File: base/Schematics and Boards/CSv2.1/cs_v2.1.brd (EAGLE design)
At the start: 38.1 x 44.5 mm, 80 parts, among them J101 J-JTAG-CORTEX-NEEDLE6-LEGS, J301 HIROSE-DF40_44-PIN_CONNECTORS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, J302 HIROSE-DF40_30-PIN_CONNECTORS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, Q201 FK3303010L, Q202 DMG3415UFY4Q-7F, Q203 FK3303010L, Q204 FK3303010L, U101 ATSAMD51, U102 AT25SF641-MHB-T, U201 COULOMB-MAX17262, U202 MAX77827BEWC+T, U203 SENSOR-SI7006, U204 LOADSWITCH-MIC94164, U205 LOADSWITCH-MIC94164, Y101 16M, Y102 ABS07-32.768KHZ-9-T

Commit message: Minor modifications from learnings of debug-board build
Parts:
- DTR, PROC, STOR, TEMP: value TPTP06R -> PTR1TP10SQ; device TestPoints:TP06R -> TestPoints:TP10SQ
- J301: value HIROSE-DF40_44-PIN_CONNECTORS-RECEPTACLE -> HIROSE-DF40_50-PIN_CONNECTORS-RECEPTACLE; device Connectors:HRS_DF40HC(3.0)-44DS-0.4V(51) -> Connectors:HRS_DF40HC(4.0)-50DS-0.4V(51)
- J302: value HIROSE-DF40_30-PIN_CONNECTORS-RECEPTACLE -> HIROSE-DF40_50-PIN_CONNECTORS-RECEPTACLE; device Connectors:HRS_DF40HC(3.0)-30DS-0.4V(51) -> Connectors:HRS_DF40HC(4.0)-50DS-0.4V(51)
- R206: value 1 -> 2.21
- moved J302 3.81 mm to (24.9, 40.5)

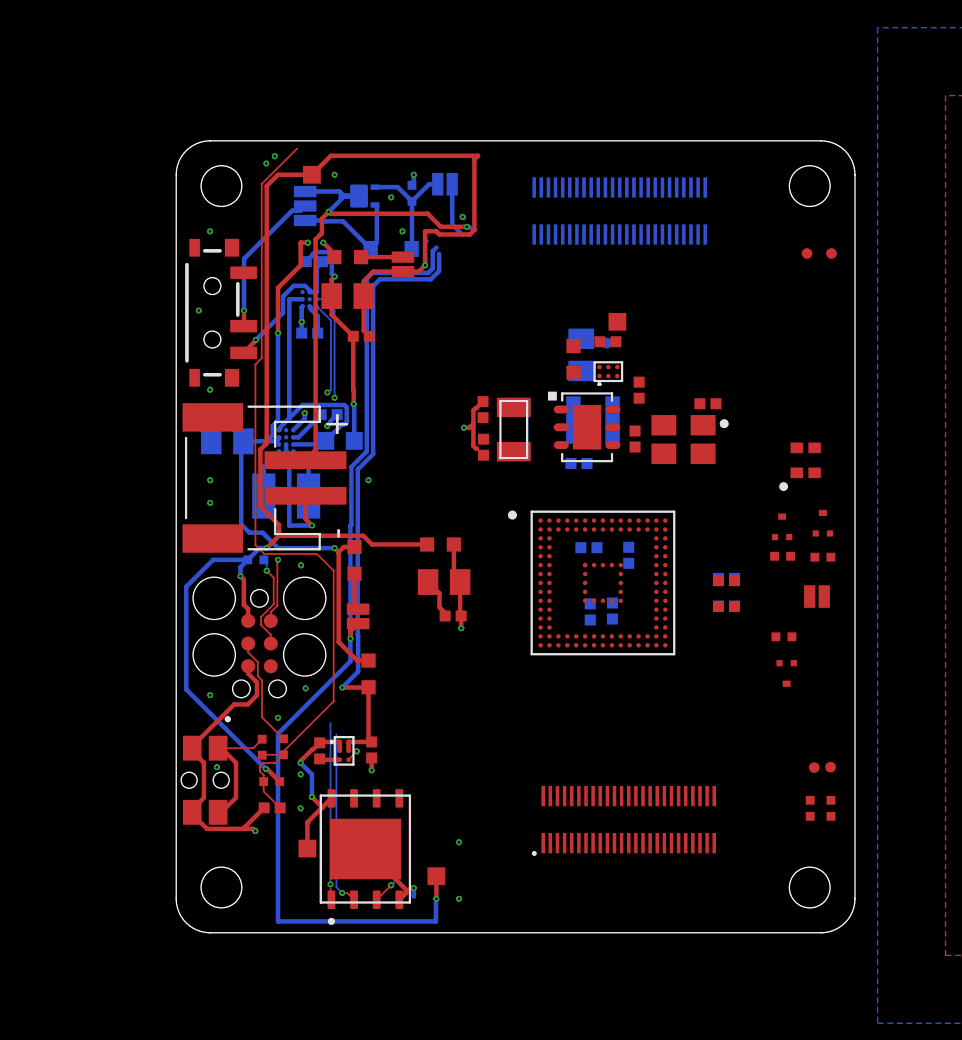
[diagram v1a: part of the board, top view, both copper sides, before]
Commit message: Revision 2.1 of schematic for the CommonSense Main Board
Changes include (at the least): Removal LED NFETs, increase connector size to 50 pins w/ 4mm z-height, swap FLASH for a Winbond part with 1 Gbit NVM, change current measurement to include two daughter card channels, add LDO as alternative to buck-boost with gating solder jumpers, modify power-switching setup to use dual PFET (one is an extension of the mechanical switch to allow higher currents), total revamp of DTR/DBG card pin-mapping, and probably a few more small items. 

These changes are local to the schematic, for the most part. Changes to the board are minimal, but do include shifting the connector up, as well as the top-most drill-holes
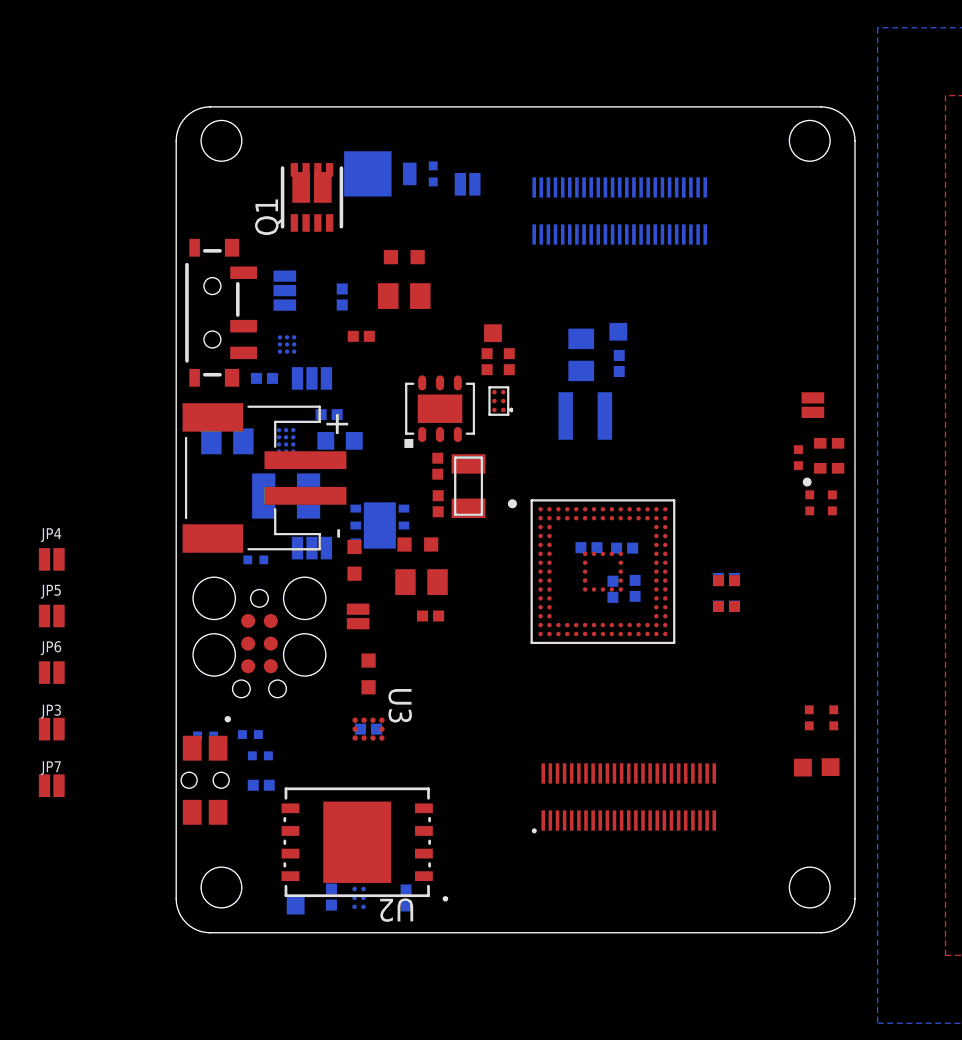
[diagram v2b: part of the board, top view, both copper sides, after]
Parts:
- removed C116, C117: 6.8p, Capacitors:C0402
- removed DTR, PROC: PTR1TP10SQ, TestPoints:TP10SQ
- removed JP204: JUMPER-SMT_2_NC_PASTE_NO-SILK, Connectors:SMT-JUMPER_2_NC_PASTE_NO-SILK
- removed Q201, Q203, Q204: FK3303010L, Switches:SSSMINI3
- removed Q202: DMG3415UFY4Q-7F, Switches:X2-DFN2015-3
- removed R205: 10, Resistors:R0603
- removed RXDBG, TXDBG: TPTP06R, TestPoints:TP06R
- removed U102: AT25SF641-MHB-T, Storage:8-UDFN
- removed Y101: 16M, Oscillators:XTAL_EPSON_TSX3225
- added C1: 0.1u, Capacitors:C0402
- added JP1, JP2: JUMPER-SMT_3_1-NC_PASTE_NO-SILK, SparkFun-Jumpers:SMT-JUMPER_3_1-NC_PASTE_NO-SILK
- added JP3, JP7: JUMPER-SMT_2_NC_PASTE_NO-SILK, Connectors:SMT-JUMPER_2_NC_PASTE_NO-SILK
- added JP4, JP5, JP6: JUMPER-SMT_2_NO_PASTEFREE, Connectors:SMT-JUMPER_2_NO_PASTEFREE_NO-SILK
- added Q1: SIS903DN, Switches:POWERPACK1212_SIS903DN
- added U1: NCP708MU330TAG, Regulators:UDFN6_NCP708]
- added U2: W25N01GVZEIG, Storage:WSON-8_W15N
- added U3: TS3A24159YZPR, Switches:DSBGA10
- CPU, SCL, SDA: value TPTP06R -> PTR1TP10SQ; device TestPoints:TP06R -> TestPoints:TP10SQ
- D201: value CUS520H3F -> MBRM110ET1G; device Diodes:CUS520H3F -> Diodes:DO-216AA_ONS
- moved JP202 10.7 mm to (35.7, 29.6), turned to 90 degrees
- moved C208 9.58 mm to (12.9, 1.96), flipped to the bottom
- moved C206 8.56 mm to (8.71, 2.01), flipped to the bottom
- moved U203 8.32 mm to (14.8, 29.4), turned to 90 degrees
- moved U204 8.30 mm to (10.3, 1.96), flipped to the bottom
- moved R203 7.66 mm to (35.6, 24.1), turned to 270 degrees
- moved C209 7.46 mm to (18.7, 32.1)
- moved TEMP 7.01 mm to (17.8, 33.7)
- moved C207 6.87 mm to (17.4, 32.1), turned to 90 degrees
- moved U205 6.36 mm to (18.1, 29.8), turned to 180 degrees
- moved C103 6.05 mm to (24.9, 32.0), turned to 270 degrees
- moved R204 5.61 mm to (34.9, 26.7), turned to 270 degrees
- moved R103 5.08 mm to (36.9, 12.1), turned to 90 degrees
- moved R104 5.08 mm to (35.5, 12.1), turned to 90 degrees
- moved JP203 4.89 mm to (6.10, 36.0), turned to 270 degrees
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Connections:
- net DTR_V_SENSE- renamed DTR_MSTR_GPIO1
- removed net +3V3_DTR_SENSE: JP205.2, R207.2
- removed net +3V3_PROC_SENSE: JP204.2, R206.2
- removed net +3V3_STOR_SENSE: C206.1, J302.18, R208.2, U204.A2, U204.B2
- removed net +3V3_TEMP_SENSE: C207.1, J302.20, R205.2, U205.A2, U205.B2
- removed net DTR_BUS0_AIN0: J301.8, U101.PA02
- removed net DTR_BUS0_AIN1: J301.16, U101.PA03
- removed net DTR_BUS0_GPIO0: J301.24, U101.PB12
- removed net DTR_BUS0_GPIO1: J301.32, U101.PB13
- removed net DTR_BUS0_SERCOM0_P0: J301.7, U101.PA08
- removed net DTR_BUS0_SERCOM0_P1: J301.15, U101.PA09
- removed net DTR_BUS0_SERCOM0_P2: J301.23, U101.PA10
- removed net DTR_BUS0_SERCOM0_P3: J301.31, U101.PA11
- removed net DTR_BUS1_AIN0: J301.10, U101.PA04
- removed net DTR_BUS1_AIN1: J301.18, U101.PA05
- removed net DTR_BUS2_AIN0: J301.12, U101.PC02
- removed net DTR_BUS2_AIN1: J301.20, U101.PC03
- removed net DTR_BUS3_AIN0: J301.14, U101.PB04
- removed net DTR_BUS3_AIN1: J301.22, U101.PB05
- removed net DTR_BUS3_GPIO0: J301.30, U101.PA06
- removed net DTR_BUS3_GPIO1: J301.38, U101.PA07
- removed net DTR_BUS3_SERCOM7_P0: J301.13, U101.PD08
- removed net DTR_BUS3_SERCOM7_P1: J301.21, U101.PD09
- removed net DTR_BUS3_SERCOM7_P2: J301.29, U101.PD10
- removed net DTR_BUS3_SERCOM7_P3: J301.37, U101.PD11
- removed net DTR_DETECT: J301.39, U101.PA21
- removed net DTR_MASTER_I2C_SCL: J301.40, R103.1, SCL.TP, U101.PA23, U201.B1, U203.6
- removed net DTR_MASTER_I2C_SDA: J301.42, R104.1, SDA.TP, U101.PA22, U201.C1, U203.1
- removed net DTR_MASTER_IRQ: J301.44
- removed net N$16: Q203.3, R203.2
- removed net STOR_HOLD: U101.PB07, U102.7
- removed net STOR_SPI5_MISO: U101.PB03, U102.2
- removed net STOR_SPI5_MOSI: U101.PB00, U102.5
- removed net STOR_SPI5_NCS: U101.PB02, U102.1
- removed net STOR_SPI5_SCK: U101.PB01, U102.6
- removed net STOR_WP: U101.PB06, U102.3
- removed net VDD_DBG: J302.2, J302.4, JP201.2
- removed net VDD_SW_IN: JP203.2, S201.2
- removed net XIN: C116.1, U101.PB22, Y101.1
- removed net XOUT: C117.1, U101.PB23, Y101.3
- new net +3V3_DTR_SENSE-: JP205.2, JP5.2, R207.2, U3.A1, U3.A3, U3.C1
- new net DBG_DTR_V_SENSE: J301.8, J302.18
- new net DBG_DTR_V_SENSE_EX: J302.20, U3.C3
- new net DBG_GPIO10: J302.40, U101.PB28
- new net DBG_GPIO11: J302.38, U101.PB29
- new net DBG_GPIO4/SERCOM6_P0: J302.30, U101.PC16
- new net DBG_GPIO5/SERCOM6_P1: J302.32, U101.PC17
- new net DBG_GPIO6/SERCOM6_P2: J302.34, U101.PC18
- new net DBG_GPIO7/SERCOM6_P3: J302.36, U101.PC19
- new net DBG_GPIO8: J302.44, U101.PB26
- new net DBG_GPIO9: J302.42, U101.PB27
- new net DBG_PROC_V_SENSE: J302.16, JP6.2, JP7.2, R206.2
- new net DBG_STOR_V_SENSE: C206.1, J302.22, JP4.2, R208.2, U204.A2, U204.B2
- new net DBG_VDD: J302.2, J302.4, J302.6, JP201.2
- new net DTR_BUS0_AIN0/GPIO2: J301.7, U101.PA02
- new net DTR_BUS0_AIN1/GPIO3: J301.9, U101.PA03
- new net DTR_BUS0_GPIO0/I2S_SCK0: J301.19, U101.PB16
- new net DTR_BUS0_GPIO1/I2S_MCK0: J301.21, U101.PB17
- new net DTR_BUS0_SERCOM5_P0/I2S_FS1: J301.42, U101.PA23
- new net DTR_BUS0_SERCOM5_P1/I2S_SDI: J301.40, U101.PA22
- new net DTR_BUS0_SERCOM5_P2/I2S_FS0: J301.30, U101.PA20
- new net DTR_BUS0_SERCOM5_P3/I2S_SDO: J301.28, U101.PA21
- new net DTR_BUS1_AIN0/GPIO2: J301.11, U101.PA04
- new net DTR_BUS1_AIN1/GPIO3: J301.13, U101.PA05
- new net DTR_BUS2_AIN0/GPIO2: J301.15, U101.PC02
- new net DTR_BUS2_AIN1/GPIO3: J301.17, U101.PC03
- new net DTR_DETECT/DTR_IRQ0/SERCOM7_P2: J301.16, U101.PD10
- new net DTR_IRQ1/SERCOM7_P3: J301.18, U101.PD11
- new net DTR_MSTR_GPIO0: J301.41, U101.PC15
- new net DTR_MSTR_GPIO_1: U101.PC20
- new net DTR_MSTR_I2C_SCL_SERCOM7_P1: J301.14, R103.1, SCL.TP, U101.PD09, U201.B1, U203.6
- new net DTR_MSTR_I2C_SDA_SERCOM7_P0: J301.12, R104.1, SDA.TP, U101.PD08, U201.C1, U203.1
- new net DTR_MSTR_SPI_CSS0_SERCOM3_P2: J301.37, U101.PD20
- new net DTR_MSTR_SPI_CSS1: J301.31, U101.PD12
- new net DTR_MSTR_SPI_MISO_SERCOM3_P3: J301.39, U101.PD21
- new net DTR_MSTR_SPI_MOSI_SERCOM3_P0: J301.33, U101.PC23
- new net DTR_MSTR_SPI_SCK_SERCOM3_P1: J301.35, U101.PC22
- new net DTR_SENSE_SW: U101.PC07, U3.B1, U3.B3
- new net DTR_V_SENSE_EX: J301.10, U3.D3
- new net N$11: Q1.4, S201.2
- new net N$3: JP2.1, U202.C2, U202.C3
- new net N$7: JP1.3, U1.1, U1.6
- new net N$8: JP203.2, Q1.10, Q1.5, Q1.6, S201.1
- new net STOR_QSPI_CK: U101.PB10, U2.6
- new net STOR_QSPI_CS: U101.PB11, U2.1
- new net STOR_QSPI_D0: U101.PA08, U2.5
- new net STOR_QSPI_D1: U101.PA09, U2.2
- new net STOR_QSPI_D2: U101.PA10, U2.3
- new net STOR_QSPI_D3: U101.PA11, U2.7
- new net VREG_BB_IN: JP1.1, U202.A2, U202.C4
- net +3V3: now also C207.1, J302.14, JP2.2, JP3.2, JP4.1, JP5.1, JP6.1, U205.A2, U205.B2, U3.D1; no longer J302.12, R205.1, U202.C2, U202.C3
- net +3V3_DTR: no longer DTR.TP, J302.16
- net +3V3_PROC: now also JP7.1; no longer J302.14, JP204.1, PROC.TP
- net +3V3_STOR: now also U2.8; no longer U102.8
- net +3V7_BATT: now also J302.12, JP203.1, Q1.7, Q1.8, Q1.9; no longer J302.6, JP203.3, Q202.3-1, Q202.3-2
- net CC_IN: now also Q1.3; no longer S201.1
- net DBG_GPIO0: now also J302.31, U101.PB22; no longer J302.7, U101.PC16
- net DBG_GPIO1: now also J302.29, U101.PB23; no longer J302.9, U101.PC17
- net DBG_GPIO2: now also J302.27, U101.PB24; no longer J302.11, U101.PC18
- net DBG_GPIO3: now also J302.25, U101.PB25; no longer J302.13, U101.PC19
- net DBG_SERIAL_RX_SERCOM4: now also J302.9; no longer J302.17, RXDBG.TP
- net DBG_SERIAL_TX_SERCOM4: now also J302.11; no longer J302.15, TXDBG.TP
- net DBG_SWCLK: now also J302.28; no longer J302.19
- net DBG_SWDIO: now also J302.26; no longer J302.21
- net DBG_TRACE_CLK: now also J302.23; no longer J302.26
- net DBG_TRACE_D0: now also J302.15; no longer J302.23
- net DBG_TRACE_D1: now also J302.17; no longer J302.25
- net DBG_TRACE_D2: now also J302.19; no longer J302.27
- net DBG_TRACE_D3: now also J302.21; no longer J302.29
- net DBG_TRACE_SWO: now also J302.13; no longer J302.28
- net DBG_USB_D_N: now also J302.49; no longer J302.22
- net DBG_USB_D_P: now also J302.47; no longer J302.24
- net DTR_BUS1_GPIO0: now also J301.23, U101.PC11; no longer J301.26, U101.PB14
- net DTR_BUS1_GPIO1: now also J301.25, U101.PC12; no longer J301.34, U101.PB15
- net DTR_BUS1_SERCOM1_P0: now also J301.38; no longer J301.9
- net DTR_BUS1_SERCOM1_P1: now also J301.36; no longer J301.17
- net DTR_BUS1_SERCOM1_P2: now also J301.26; no longer J301.25
- net DTR_BUS1_SERCOM1_P3: now also J301.24; no longer J301.33
- net DTR_BUS2_GPIO0: now also J301.27, U101.PC13; no longer J301.28, U101.PB16
- net DTR_BUS2_GPIO1: now also J301.29, U101.PC14; no longer J301.36, U101.PB17
- net DTR_BUS2_SERCOM2_P0: now also J301.34; no longer J301.11
- net DTR_BUS2_SERCOM2_P1: now also J301.32; no longer J301.19
- net DTR_BUS2_SERCOM2_P2: now also J301.22; no longer J301.27
- net DTR_BUS2_SERCOM2_P3: now also J301.20; no longer J301.35
- net EN_TEMP: now also U101.PB02; no longer U101.PB25
- net GND: now also C1.2, J302.7, S201.3, U1.2, U1.3, U1.7, U2.4, U2.9, U3.A2; no longer C116.2, C117.2, Q201.2, Q203.2, Q204.2, U102.4, U102.9, Y101.2, Y101.4
- net LED_B: now also R202.2, U101.PB18; no longer Q201.1, U101.PB28
- net LED_G: now also R203.2, U101.PB19; no longer Q203.1, U101.PB27
- net LED_R: now also R204.2, U101.PB20; no longer Q204.1, U101.PB26
- net N$15: now also JP2.3, U1.4, U1.5; no longer Q201.3, R202.2
- net N$17: now also C1.1, JP3.1, U3.D2; no longer Q204.3, R204.2
- net NRESET: now also J302.24; no longer J302.30
- net VDD_DBG_JMP: now also D201.1, Q1.2; no longer D201.P, Q202.1
- net VDD_SW: now also D201.2, JP203.3, Q1.1; no longer D201.N, JP203.1, Q202.2
- net VREG_IN: now also JP1.2; no longer U202.A2, U202.C4
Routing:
- net +3V3_PROC: track 82.1 -> 0.00 mm, vias 4 -> 0
- net +3V3_DTR: track 55.8 -> 0.00 mm, vias 2 -> 0
- net GND: track 54.1 -> 0.00 mm, vias 29 -> 0
- net NRESET: track 45.3 -> 0.00 mm
- net +3V3: track 44.2 -> 0.00 mm, vias 5 -> 0
- net +3V3_STOR_SENSE: track 34.6 -> 0.00 mm, vias 1 -> 0
- net DBG_SWCLK: track 29.4 -> 0.00 mm, vias 2 -> 0
- net +3V7_BATT: track 27.2 -> 0.00 mm, vias 2 -> 0
- net DBG_SWDIO: track 26.5 -> 0.00 mm, vias 2 -> 0
- net VREG_IN: track 16.3 -> 0.00 mm
- net STOR_SPI5_NCS: track 9.93 -> 0.00 mm, vias 1 -> 0
- net STOR_SPI5_MISO: track 9.85 -> 0.00 mm, vias 1 -> 0
- net +3V3_STOR: track 9.62 -> 0.00 mm, vias 2 -> 0
- net VDD_SW_IN: track 8.45 -> 0.00 mm, vias 1 -> 0
- net CC_IN: track 8.29 -> 0.00 mm, vias 1 -> 0
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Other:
- board size 38.1 x 44.5 mm -> 38.1 x 46.4 mm

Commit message: Upgrade power selection on main board from PFET -> 2:1 power mux
Testing on CSmain 2.0 showed some disturbing changes in voltage across the PFET (most likely due to an device physics imposing a typical Vgs threshold before conducting well) that would make the LDO on the board unusable if only a LiPo battery was available. For boards that will need power switching between main board source and debug-board source, we need something more sophisticated. 

Also included is a load switch whose enable is controlled by a mechanical switch. This should be more trustworthy than a PFET, and can conduct substantially more current than the mechanical switch alone.
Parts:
- removed D201: MBRM110ET1G, Diodes:DO-216AA_ONS
- removed Q1: SIS903DN, Switches:POWERPACK1212_SIS903DN
- added C2, C3, C4: 1u, Capacitors:C0402
- added C5: 4.7u, Capacitors:C0805
- added D1, D2: CUS520H3F, Diodes:CUS520H3F
- added U4: LOADSWITCH-MIC94164, Switches:WLCSP6_2X3
- added U5: FPF1321UCX, Switches:BGA6N50P3X2_146X96X62N
- R201: value 10M -> 1M
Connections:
- removed net VDD_DBG_JMP: D201.1, JP201.1, Q1.2, R201.2
- removed net VDD_SW: D201.2, JP203.3, Q1.1
- new net V_SEL_EN: D1.N, D2.N, U5.A1
- new net V_SEL_IN_B: C4.1, D2.P, JP201.1, R201.2, U5.B1, U5.C2
- new net V_SEL_OUT: C5.1, JP203.1, U5.B2
- net +3V7_BATT: now also C3.1, D1.P, JP203.3, U5.A2; no longer JP203.1, Q1.7, Q1.8, Q1.9
- net CC_IN: now also U4.A1, U4.B1; no longer Q1.3
- net GND: now also C2.2, C3.2, C4.2, C5.2, S201.1, U4.C1, U5.C1; no longer S201.3
- net N$11: now also U4.C2; no longer Q1.4
- net N$8: now also C2.1, S201.3, U4.A2, U4.B2; no longer Q1.10, Q1.5, Q1.6, S201.1

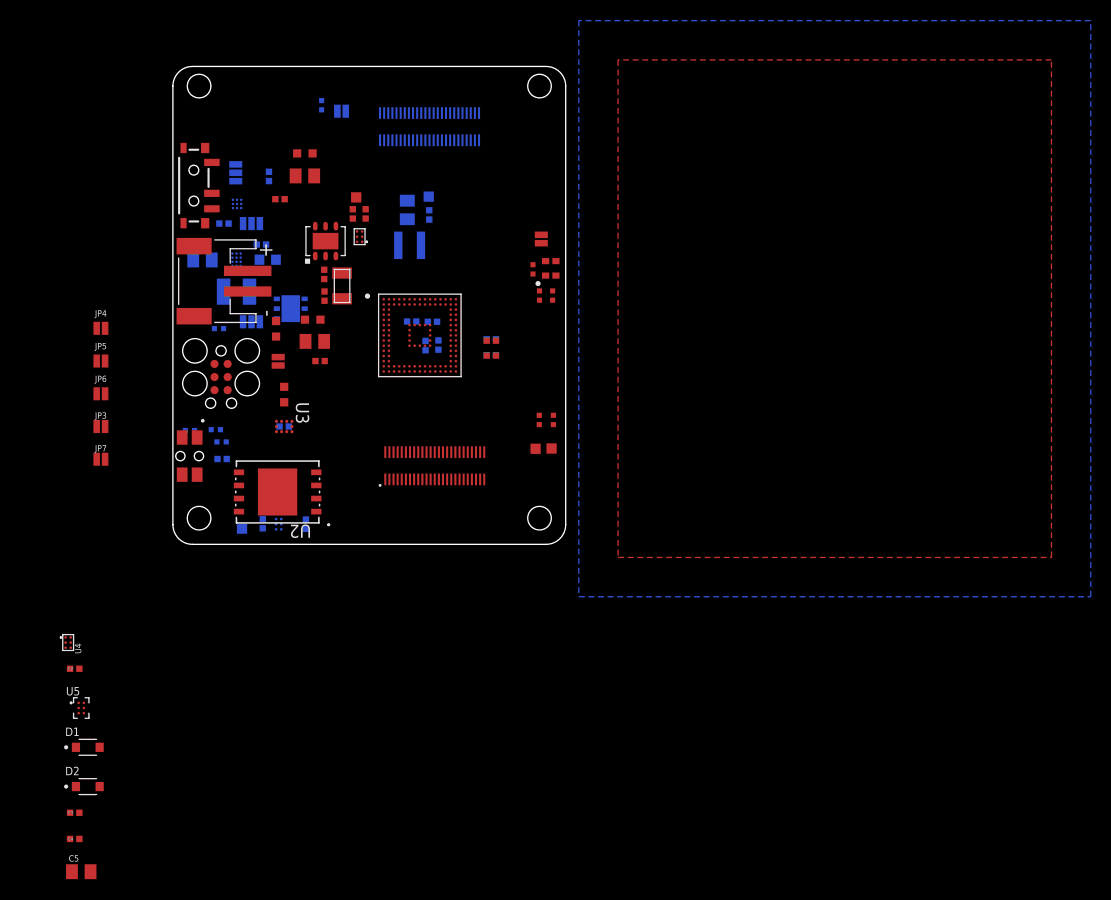
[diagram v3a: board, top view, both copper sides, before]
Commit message: Swap daughter card v-sense pins
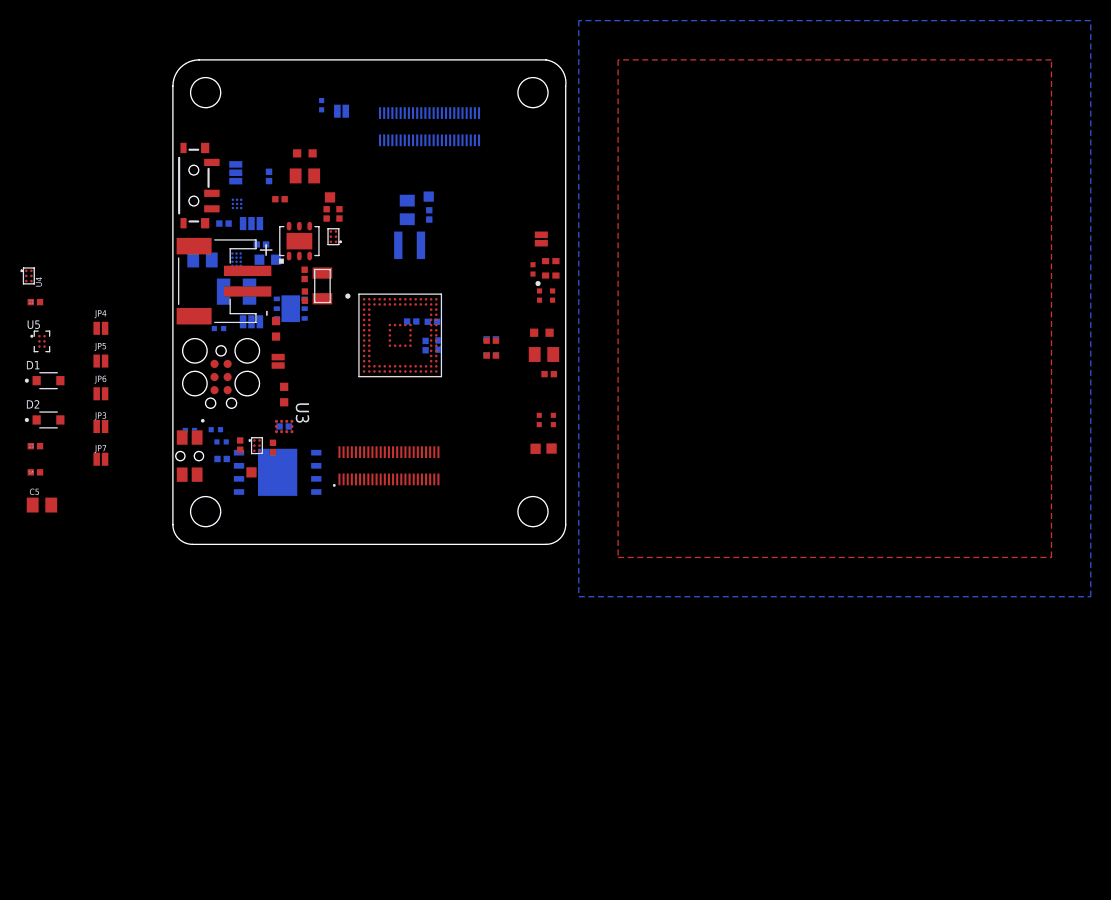
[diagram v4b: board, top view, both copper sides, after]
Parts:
- moved C2 35.8 mm to (-13.3, 23.5)
- moved C3 35.8 mm to (-13.3, 9.53)
- moved C4 35.8 mm to (-13.3, 6.99)
- moved C5 35.8 mm to (-12.7, 3.81)
- moved D1 35.8 mm to (-12.1, 15.9)
- moved D2 35.8 mm to (-12.1, 12.1)
- moved U4 35.8 mm to (-14.0, 26.0)
- moved U5 35.8 mm to (-12.7, 19.7)
- moved C108 22.3 mm to (36.5, 16.5)
- moved L102 22.3 mm to (35.8, 20.5)
- moved C110 22.3 mm to (36.0, 18.4)
- moved C208 8.10 mm to (9.70, 9.40), flipped to the top
- moved C206 7.93 mm to (6.53, 9.63), flipped to the top
- moved U204 7.91 mm to (8.15, 9.58), flipped to the top
- moved STOR 5.54 mm to (7.62, 6.99), flipped to the top, turned to 180 degrees
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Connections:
- removed net DBG_DTR_V_SENSE: J301.8, J302.18
- removed net DBG_DTR_V_SENSE_EX: J302.20, U3.C3
- removed net DTR_V_SENSE_EX: J301.10, U3.D3
- new net DBG_DTR0_V_SENSE: J302.18, U3.C3
- new net DBG_DTR1_V_SENSE: J301.10, J302.20
- new net DTR_DTR0_V_SENSE: J301.8, U3.D3
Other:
- board size 38.1 x 46.4 mm -> 38.1 x 47 mm

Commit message: Finished schematic revision for main, debug boards.
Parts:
- removed C3, C4: 1u, Capacitors:C0402
- removed C5: 4.7u, Capacitors:C0805
- removed D1, D2: CUS520H3F, Diodes:CUS520H3F
- removed JP4, JP5, JP6: JUMPER-SMT_2_NO_PASTEFREE, Connectors:SMT-JUMPER_2_NO_PASTEFREE_NO-SILK
- removed R201: 1M, Resistors:R0402
- added Q1: DMG3415UFY4Q-7F, Switches:X2-DFN2015-3
- added R1: 510k, Resistors:R0402
- U5: value FPF1321UCX -> PD3S140-7; device Switches:BGA6N50P3X2_146X96X62N -> Diodes:POWERDI323
- moved U5 28.6 mm to (-11.4, -8.89)
- moved J302 3.59 mm to (21.6, 41.9)
- moved R206 2.54 mm to (10.3, 37.9)
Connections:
- net DBG_TRACE_CLK renamed DBG_TRACE_CLK/GPIO17
- net DBG_TRACE_D0 renamed DBG_TRACE_D0/GPIO13
- net DBG_TRACE_D1 renamed DBG_TRACE_D1/GPIO14
- net DBG_TRACE_D2 renamed DBG_TRACE_D2/GPIO15
- net DBG_TRACE_D3 renamed DBG_TRACE_D3/GPIO16
- net DBG_TRACE_SWO renamed DBG_TRACE_SWO/GPIO12
- net N$11 renamed V.SRC.EN
- net N$8 renamed V.SRC
- removed net V_SEL_EN: D1.N, D2.N, U5.A1
- removed net V_SEL_OUT: C5.1, JP203.1, U5.B2
- new net +3V3_DTR.SW: JP205.2, U3.C1
- new net N$2: JP203.3, Q1.2, U5.2
- net +3V3: no longer JP4.1, JP5.1, JP6.1
- net +3V3_DTR_SENSE-: no longer JP205.2, JP5.2, U3.C1
- net +3V7_BATT: now also JP203.1, Q1.3-1, Q1.3-2; no longer C3.1, D1.P, JP203.3, U5.A2
- net DBG_PROC_V_SENSE: no longer JP6.2
- net DBG_STOR_V_SENSE: no longer JP4.2
- net GND: now also R1.1; no longer C3.2, C4.2, C5.2, R201.1, S201.1, U5.C1
- net V_SEL_IN_B: now also Q1.1, R1.2, U5.1; no longer C4.1, D2.P, R201.2, U5.B1, U5.C2
